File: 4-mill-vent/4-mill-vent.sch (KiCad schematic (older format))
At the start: 78 parts, among them J1 Fan, J2 Buzzer, J3 Power, J4 ICSP, Q1 MMBT3904, Q2 MMBT3904, Q3 PZT3904, Q4 PZT3904, Q5 TSM480P06CP, Q6 MMBT3904, Q7 MMBT3904, SW1 Power_off, SW2 Power_On, SW3 Fan_Down, SW4 Fan_Up, U1 LM321, U2 ATmega328P-AU, U3 TPSM84212EAB, U4 LM1117-5.0, Y1 16.000MHZ

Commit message: BOM started
More updates to board
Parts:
- removed Motor1: Mounting Holes, Connector_PinHeader_2.54mm:PinHeader_1x02_P2.54mm_Vertical, symbol Connector:Conn_01x02_Male
- added H1, H2: MountingHole_Pad, symbol Mechanical:MountingHole_Pad
- D1, D11, D12, D14, D16, D2: footprint Diode_SMD:D_1206_3216Metric -> Diode_SMD:D_SOD-123F
- D3: value 833-3SMAJ5936B-TP -> SMBJ5362B-TP
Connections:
- net at D2.1 (K), R1.2: now also H1.1
- net at D2.2 (A), Q4.2 (C): now also H2.1
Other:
- note added: "Micro_Power_Down is active High output from the Micro.\nLatching this line low will power down the unit.\n\nUp is active low input to the Micro.\nWhen low this signals the Micro the Up button is depressed.\nUp is debounced in hardware.\nDo Not USE Int Pull Up.\n\nDown is active low input to the Micro.\nWhen low this signals the Micro the Down button is depressed.\nUp is debounced in hardware.\nDo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"
- note removed: "Micro_Power_Down is active High output from the Micro.\nLatching this line low will power down the unit.\n\nExt_Power is active low input to the Micro.\nWhen low this tell the Micro that an Ext Batt is in use.\nDo Not USE Int Pull Up.\n\nUp is active low input to the Micro.\nWhen low this signals the Micro the Up button is depressed.\nUp is debounced in hardware.\nDo Not USE Int Pull Up.\n\nDown 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"
- moved on the sheet: C1, D1, D2, D3, F1, J1, J2, J3, Q1, Q2, Q3, Q4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

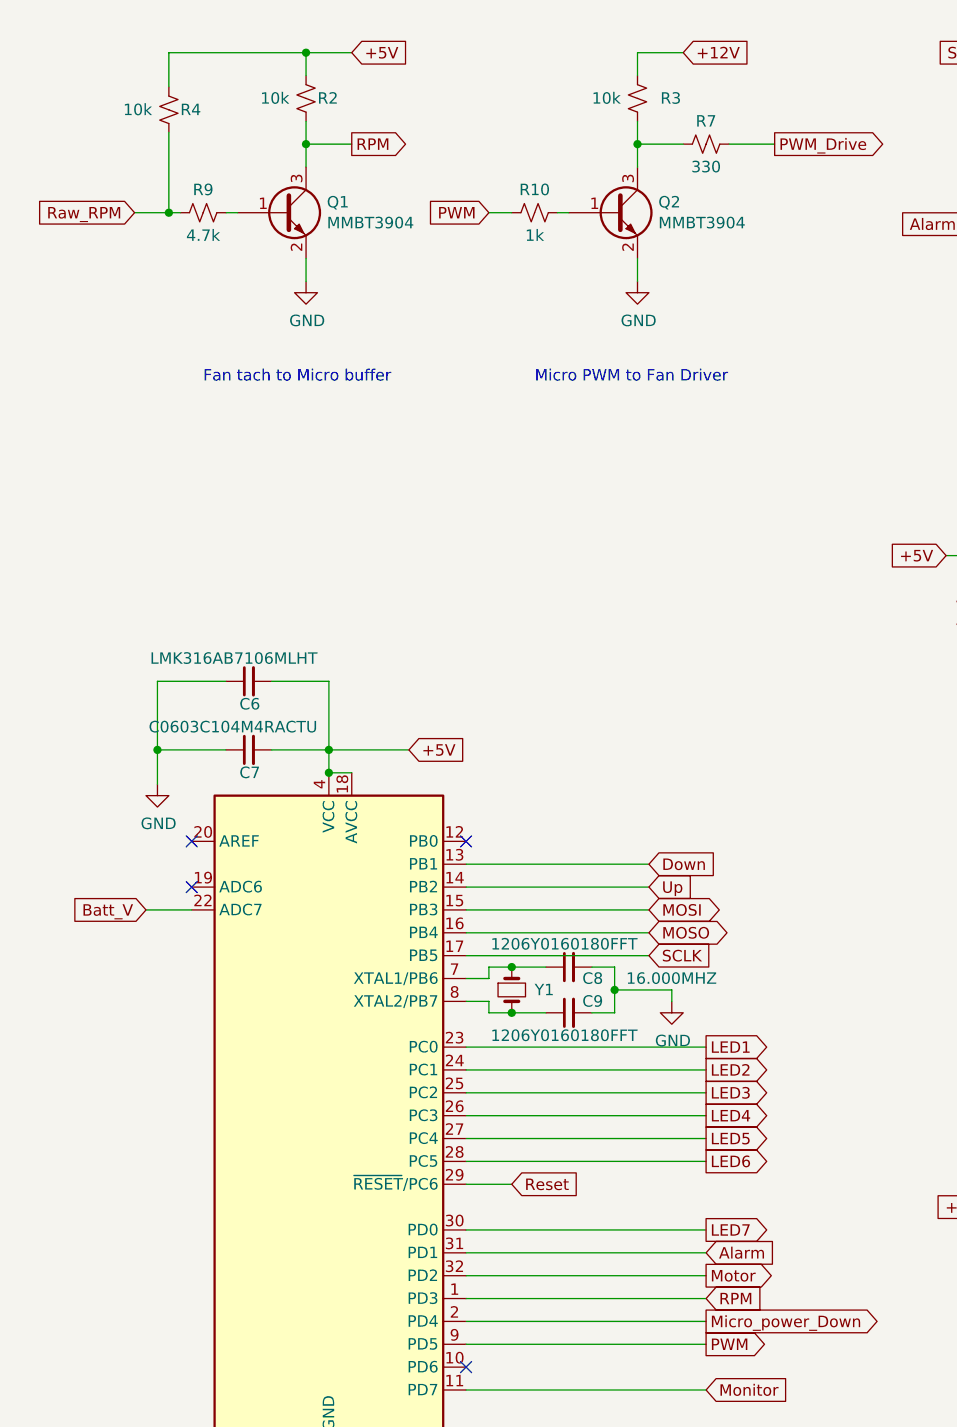
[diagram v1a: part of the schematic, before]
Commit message: more updates
Found i added a extra resistor to raw_rpm, moved a few pins around the micro.. misc. clean up
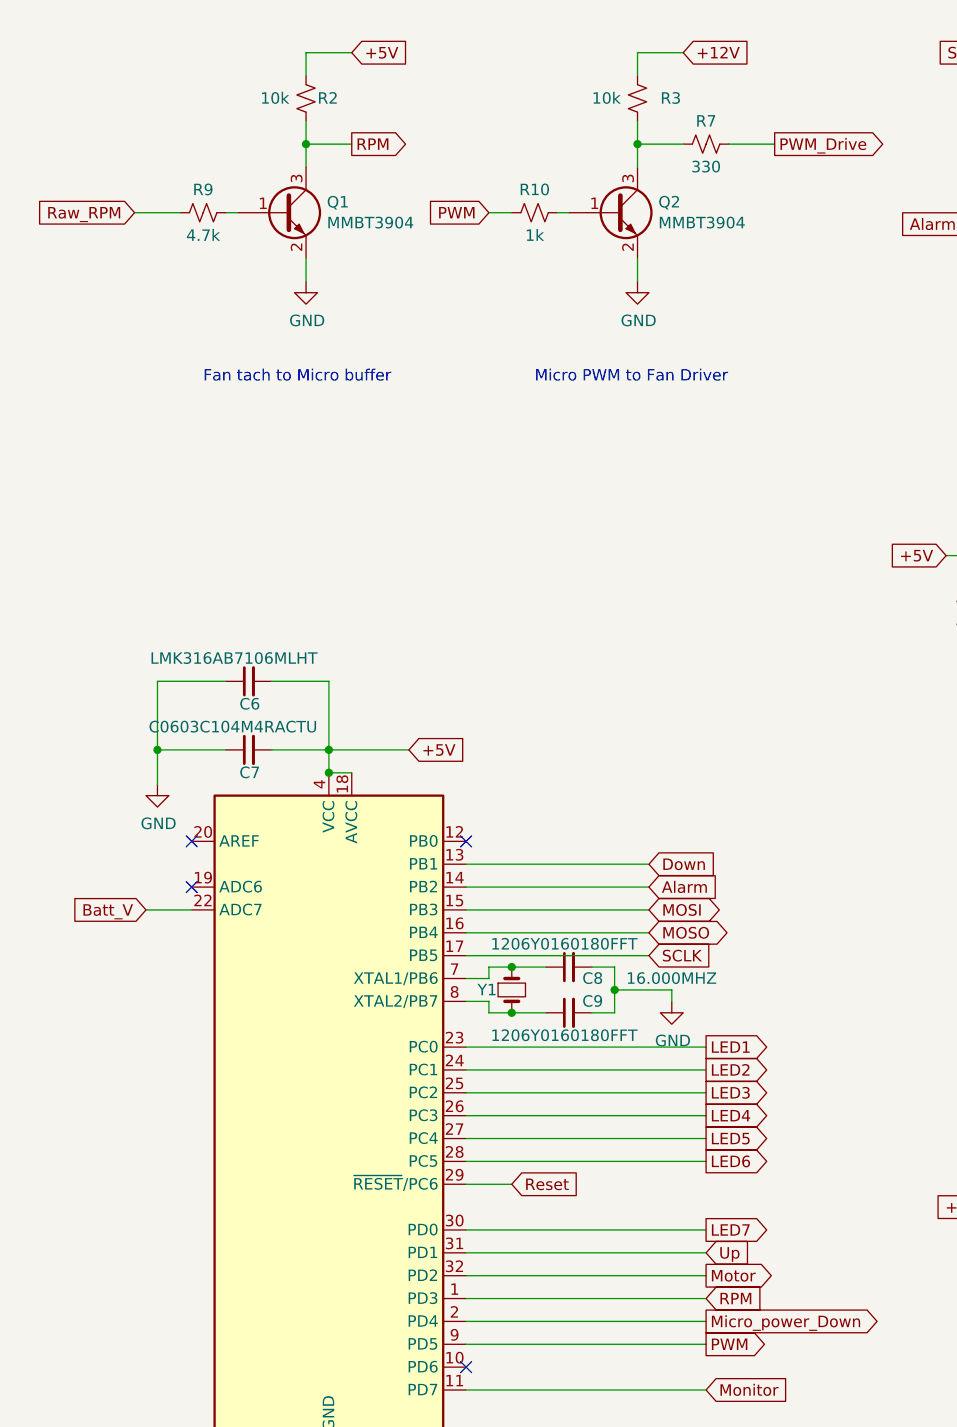
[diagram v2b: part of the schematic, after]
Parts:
- removed R4: 10k, Resistor_SMD:R_0603_1608Metric, symbol Device:R_Small_US
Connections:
- net Alarm: now also U2.14 (PB2); no longer U2.31 (PD1)
- net Up: now also U2.31 (PD1); no longer U2.14 (PB2)
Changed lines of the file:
@@
 U 1 1 5F8CFD3F
 P 2700 4750
-F 0 "Y1" V 2700 4850 50  0000 L CNN
+F 0 "Y1" V 2700 4600 50  0000 L CNN
 F 1 "16.000MHZ" V 2650 5250 50  0000 L CNN
 F 2 "Crystal:Crystal_SMD_0603-2Pin_6.0x3.5mm" H 2700 4750 50  0001 C CNN
@@
 Text GLabel 3550 6000 2    50   Output ~ 0
 Motor
-Text GLabel 3550 5900 2    50   Input ~ 0
+Text GLabel 3300 4300 2    50   Input ~ 0
 Alarm
 Text GLabel 1100 4400 0    50   Input ~ 0
@@
 	-1   0    0    -1
 $EndComp
-Text GLabel 3300 4300 2    50   Input ~ 0
+Text GLabel 3550 5900 2    50   Input ~ 0
 Up
 $Comp
@@
 Text Notes 1150 9700 0    50   ~ 0
 Micro_Power_Down is active High output from the Micro.\nLatching this line low will power down the unit.\n\nUp is active low input to the Micro.\nWhen low this signals the Micro the Up button is depressed.\nUp is debounced in hardware.\nDo Not USE Int Pull Up.\n\nDown is active low input to the Micro.\nWhen low this signals the Micro the Down button is depressed.\nUp is debounced in hardware.\nDo Not USE Int Pull Up.\n\nRPM is an input to the Micro.\nWhen active, is a frequency directly related to fan speed\nthis should drive a counter.\nUp is debounced in hardware.\nDo Not USE Int Pull Up.\n\nMonitor is an input to the Micro.\nIt is active low and signals the micro that the power down button is being pushed.\nA diode is used to isolate the micro fron positive voltages.\nAs a result of this a PULL UP must be used on this input.
-$Comp
-L Device:R_Small_US R4
-U 1 1 5F2E620F
-P 1200 900
-F 0 "R4" H 1150 900 50  0000 R CNN
-F 1 "10k" H 1400 900 50  0000 R CNN
-F 2 "Resistor_SMD:R_0603_1608Metric" H 1200 900 50  0001 C CNN
-F 3 "~" H 1200 900 50  0001 C CNN
-	1    1200 900
-	-1   0    0    1
-$EndComp
-Wire Wire Line
-	1050 1350 1200 1350
-Wire Wire Line
-	1200 1350 1200 1000
-Connection ~ 1200 1350
-Wire Wire Line
-	1200 1350 1250 1350
-Wire Wire Line
-	1200 800  1200 650
-Wire Wire Line
-	1200 650  1800 650
-Connection ~ 1800 650
 Wire Wire Line
 	8550 5650 8950 5650
@@
 	0    1    1    0
 $EndComp
+Wire Wire Line
+	1050 1350 1250 1350
 $EndSCHEMATC

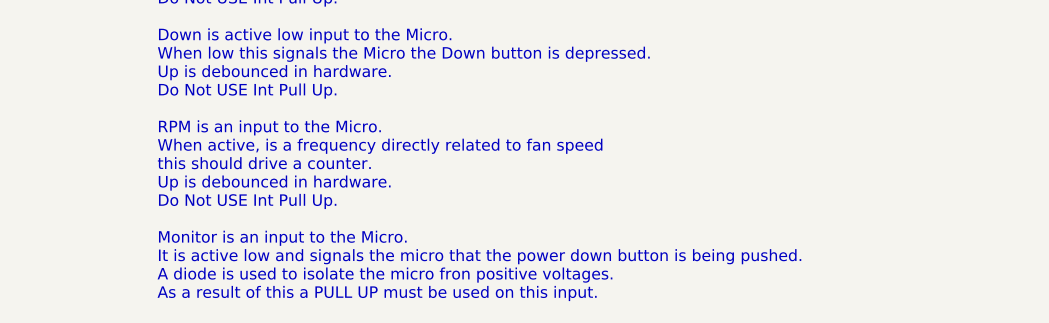
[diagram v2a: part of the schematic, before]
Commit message: Worked on moving parts around to improve ground plane
lots of parts and trace movement re-routing to make the ground plane lbetter.
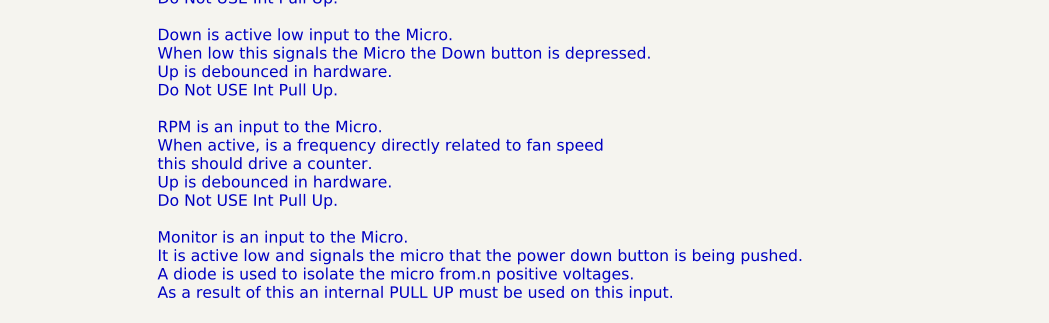
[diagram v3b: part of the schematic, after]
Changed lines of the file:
@@
 	12000 7400 12000 7550
 Text Notes 1150 9700 0    50   ~ 0
-Micro_Power_Down is active High output from the Micro.\nLatching this line low will power down the unit.\n\nUp is active low input to the Micro.\nWhen low this signals the Micro the Up button is depressed.\nUp is debounced in hardware.\nDo Not USE Int Pull Up.\n\nDown is active low input to the Micro.\nWhen low this signals the Micro the Down button is depressed.\nUp is debounced in hardware.\nDo Not USE Int Pull Up.\n\nRPM is an input to the Micro.\nWhen active, is a frequency directly related to fan speed\nthis should drive a counter.\nUp is debounced in hardware.\nDo Not USE Int Pull Up.\n\nMonitor is an input to the Micro.\nIt is active low and signals the micro that the power down button is being pushed.\nA diode is used to isolate the micro fron positive voltages.\nAs a result of this a PULL UP must be used on this input.
+Micro_Power_Down is active High output from the Micro.\nLatching this line low will power down the unit.\n\nUp is active low input to the Micro.\nWhen low this signals the Micro the Up button is depressed.\nUp is debounced in hardware.\nDo Not USE Int Pull Up.\n\nDown is active low input to the Micro.\nWhen low this signals the Micro the Down button is depressed.\nUp is debounced in hardware.\nDo Not USE Int Pull Up.\n\nRPM is an input to the Micro.\nWhen active, is a frequency directly related to fan speed\nthis should drive a counter.\nUp is debounced in hardware.\nDo Not USE Int Pull Up.\n\nMonitor is an input to the Micro.\nIt is active low and signals the micro that the power down button is being pushed.\nA diode is used to isolate the micro from.n positive voltages.\nAs a result of this an internal PULL UP must be used on this input.
 Wire Wire Line
 	8550 5650 8950 5650

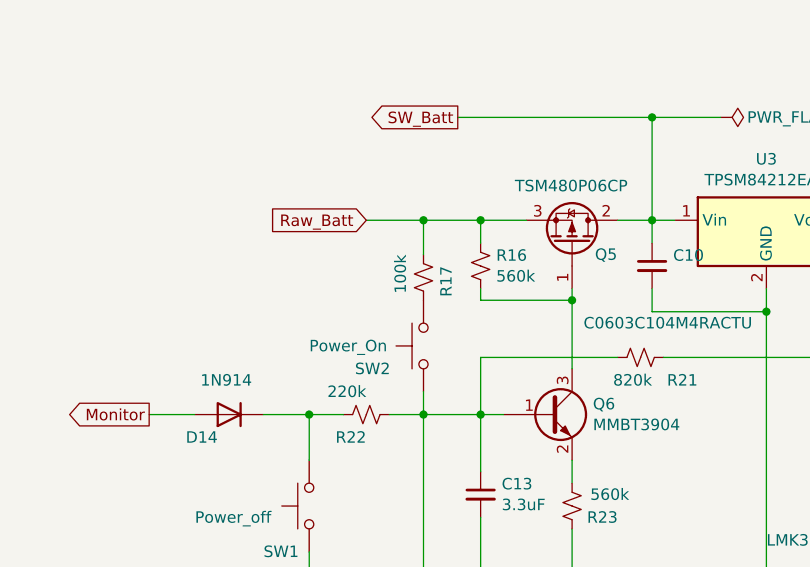
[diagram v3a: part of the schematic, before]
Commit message: just making sure the lastest is pushed
going to be doing some testing today on power down and monitor. also going to change interface with fan, as there was no problems with the design on the test board.
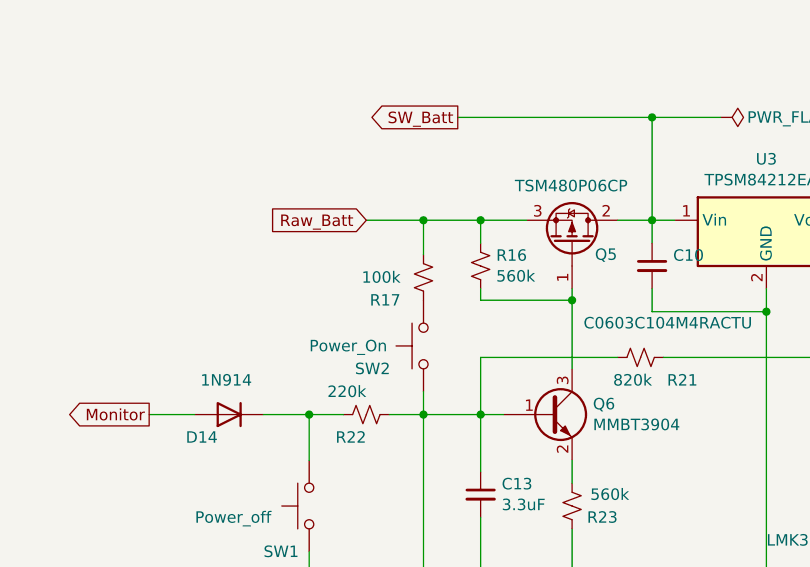
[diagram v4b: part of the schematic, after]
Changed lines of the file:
@@
 U 1 1 5F495ED6
 P 12000 5500
-F 0 "R17" V 11900 5450 50  0000 L CNN
-F 1 "100k" V 12100 5400 50  0000 L CNN
+F 0 "R17" H 12100 5600 50  0000 L CNN
+F 1 "100k" H 12100 5500 50  0000 L CNN
 F 2 "Resistor_SMD:R_0603_1608Metric" H 12000 5500 50  0001 C CNN
 F 3 "~" H 12000 5500 50  0001 C CNN

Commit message: last update for this round
last update for ver4 of board.
next will be ver5
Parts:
- removed Q1, Q2, Q7: MMBT3904, Package_TO_SOT_SMD:SOT-23, symbol Transistor_BJT:MMBT3904
- removed R10: 1k, Resistor_SMD:R_0603_1608Metric, symbol Device:R_Small_US
- removed R2, R3: 10k, Resistor_SMD:R_0603_1608Metric, symbol Device:R_Small_US
- removed R24: 4.7k, Resistor_SMD:R_0603_1608Metric, symbol Device:R_Small_US
- added C17: C0603C104M4RACTU, Capacitor_SMD:C_0603_1608Metric, symbol Device:C_Small
- H1: footprint (none) -> Connector_Molex:Molex_KK-254_AE-6410-02A_1x02_P2.54mm_Vertical
- R1: footprint Resistor_SMD:R_1206_3216Metric_Pad1.42x1.75mm_HandSolder -> Resistor_SMD:R_0612_1632Metric_Pad1.18x3.40mm_HandSolder
- R9: value 4.7k -> 1k
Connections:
- net PWM is gone; now on an unnamed net: U2.9 (PD5)
- net RPM is gone; now on an unnamed net: U2.1 (PD3)
- net GND: now also C17.2
- net Reset: now also C17.1
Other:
- note added: "Micro_Power_Down is active High output from the Micro.\nLatching this line low will power down the unit.\n\nUp is active low input to the Micro.\nWhen low this signals the Micro the Up button is depressed.\nUp is debounced in hardware.\nDo Not USE Int Pull Up.\n\nDown is active low input to the Micro.\nWhen low this signals the Micro the Down button is depressed.\nDown is debounced in hardware.\n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"
- note removed: "Fan tach to Micro buffer"
- note removed: "Micro PWM to Fan Driver"
- note removed: "Micro_Power_Down is active High output from the Micro.\nLatching this line low will power down the unit.\n\nUp is active low input to the Micro.\nWhen low this signals the Micro the Up button is depressed.\nUp is debounced in hardware.\nDo Not USE Int Pull Up.\n\nDown is active low input to the Micro.\nWhen low this signals the Micro the Down button is depressed.\nUp is debounced in hardware.\nDo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"
- note removed: "tested over 2 second delay off from full load to no load\n5v reg. set to 5.6v for diode drop."
- moved on the sheet: C1, C10, C13, C14, C15, C16, C2, C3, C4, C5, D1, D10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

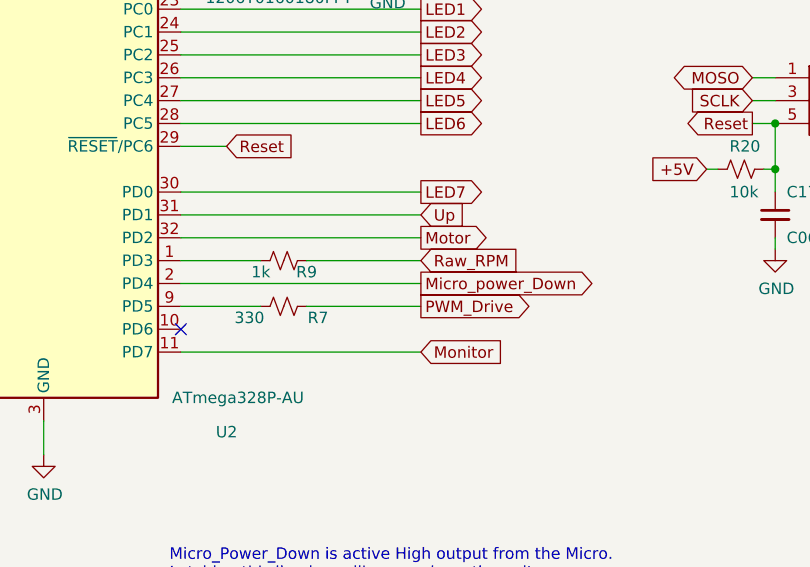
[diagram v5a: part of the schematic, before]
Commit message: And update was missed some where along the way and a reset cap was not added to the board
updated both zip and 4-mill-vent files so they are in sync.

cleaned up so grounds for the micro as well
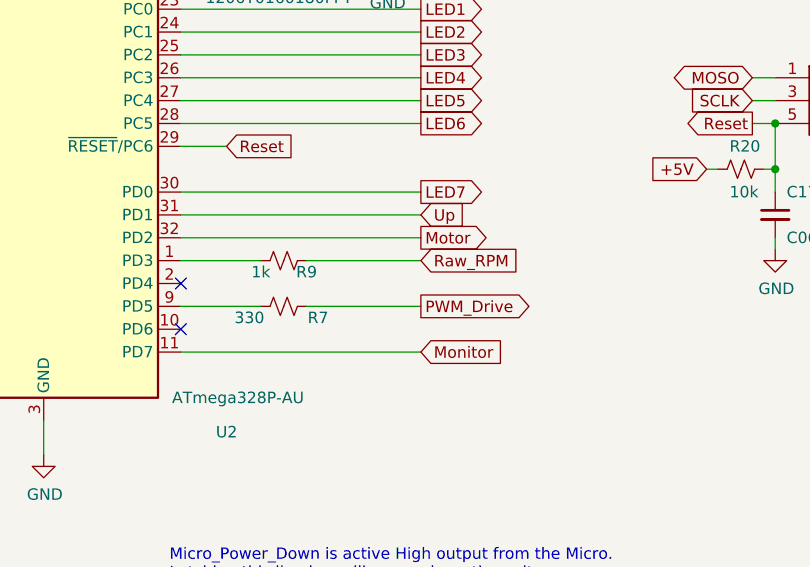
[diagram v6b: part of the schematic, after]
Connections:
- net Micro_power_Down: no longer names the net of U2.2 (PD4)
- no-connect marks 5 -> 6
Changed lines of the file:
@@
 	7150 650  7150 900
 Connection ~ 7450 650
-Text GLabel 3550 6200 2    50   Output ~ 0
-Micro_power_Down
 Wire Wire Line
 	5100 5500 5100 5700
@@
 Wire Wire Line
 	2500 6500 3550 6500
-Wire Wire Line
-	3550 6200 2500 6200
 NoConn ~ 2500 6400
 NoConn ~ 2500 4100
@@
 Wire Wire Line
 	3050 6100 3550 6100
+NoConn ~ 2500 6200
 $EndSCHEMATC
